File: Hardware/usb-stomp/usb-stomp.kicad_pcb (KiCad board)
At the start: 4 copper layers, 91 x 60 mm, 130 parts, among them J101 USB_C_Receptacle_USB2.0_16P, J102 Barrel_Jack_Switch, J103 AudioJack3_SwitchTR, J201 AudioJack4, J202 AudioJack4, J301 AudioJack3_SwitchTR, J302 AudioJack3_SwitchTR, SW101 SW_SPST, SW102 RotaryEncoder_Switch_MP, U101 USBLC6-2P6, U102 TPS62153, U103 TLV76733DRVx, U201 SN74AHCT1G125DCKR, U202 TLP2310, U301 OPA2365AIDR, U302 TLV76733DRVx, U303 TAC5242, U401 RP2354A, Y401 ABM8-272-T3

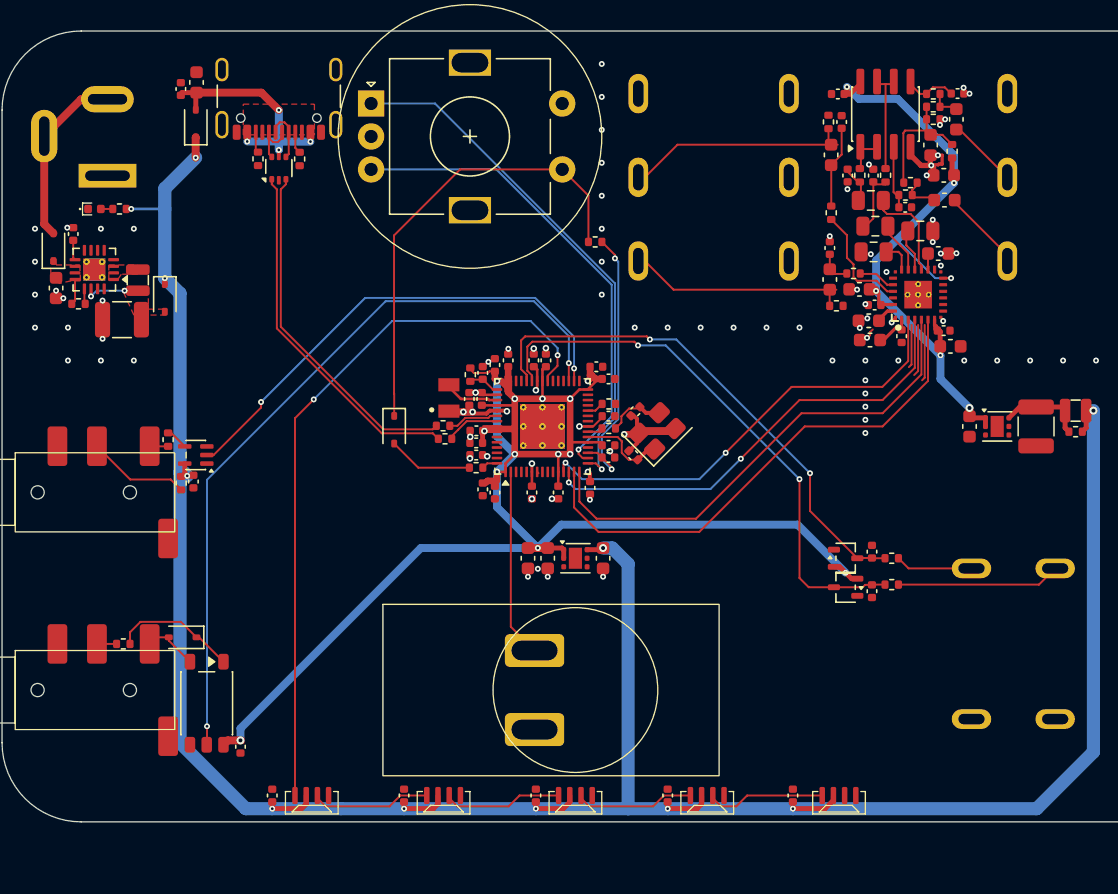
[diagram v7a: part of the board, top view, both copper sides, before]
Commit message: Various minor usb stomp pcb cleanups
Clean up traces and vias.  Add a ground keep-out area around the RP2354
crystal - it seems to have gotten lost at some point.

This is the manual cleanup after the mostly automated "move things
around".

Still DRC clean.

Signed-off-by: Linus Torvalds <torvalds@linux-foundation.org>
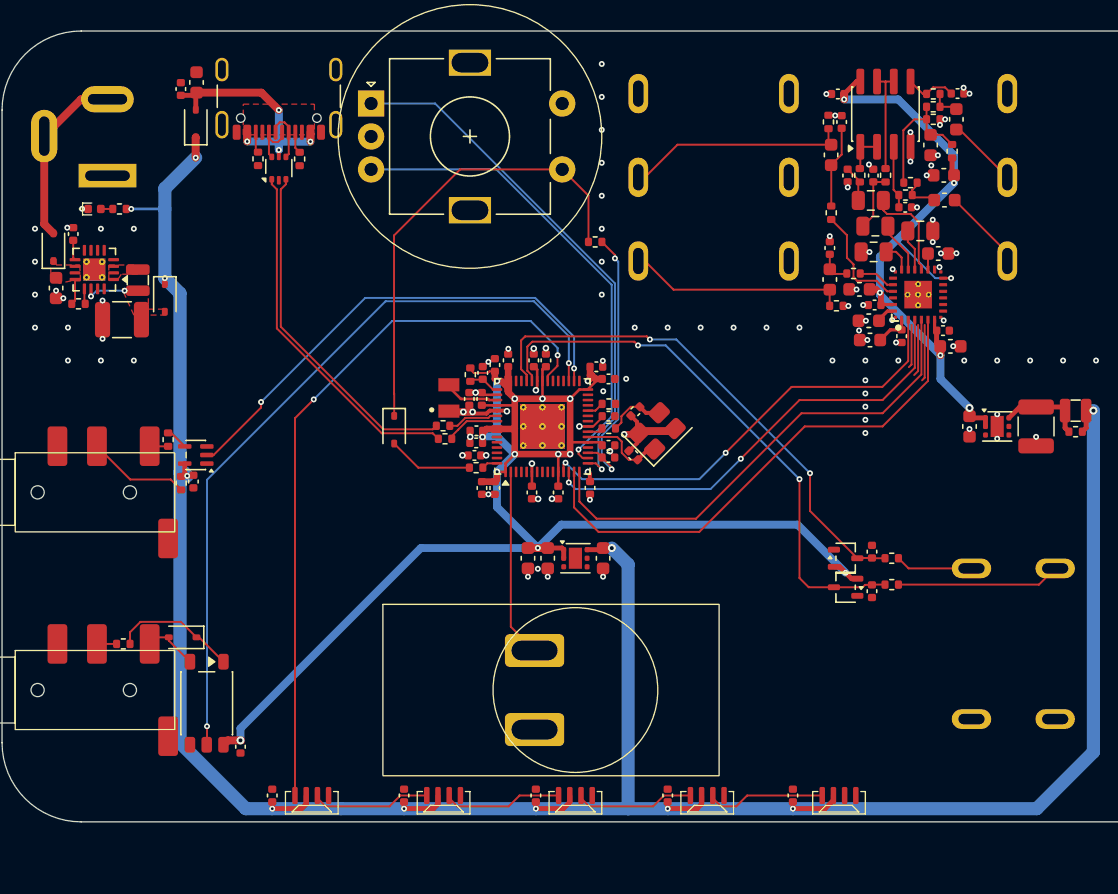
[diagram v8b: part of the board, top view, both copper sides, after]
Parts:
- moved C410 0.34 mm to (93.9, 104.7)
- moved C403 0.14 mm to (92.3, 102.2)
- moved C415 0.12 mm to (92.9, 104.7)
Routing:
- net GND: track 29.4 -> 22.0 mm, vias 84 -> 101
- net VBUS: track 17.7 -> 19.2 mm
- net +3V3: track 150.0 -> 149.2 mm
- net /TAC5242/OUT^{RIGHT}: track 17.0 -> 16.5 mm
- net /TAC5242/OUT^{LEFT}: track 16.7 -> 16.2 mm
